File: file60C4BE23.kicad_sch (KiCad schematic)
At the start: 6 parts, among them U10 PCF2123TS_1,118, Y1 32.768kHz

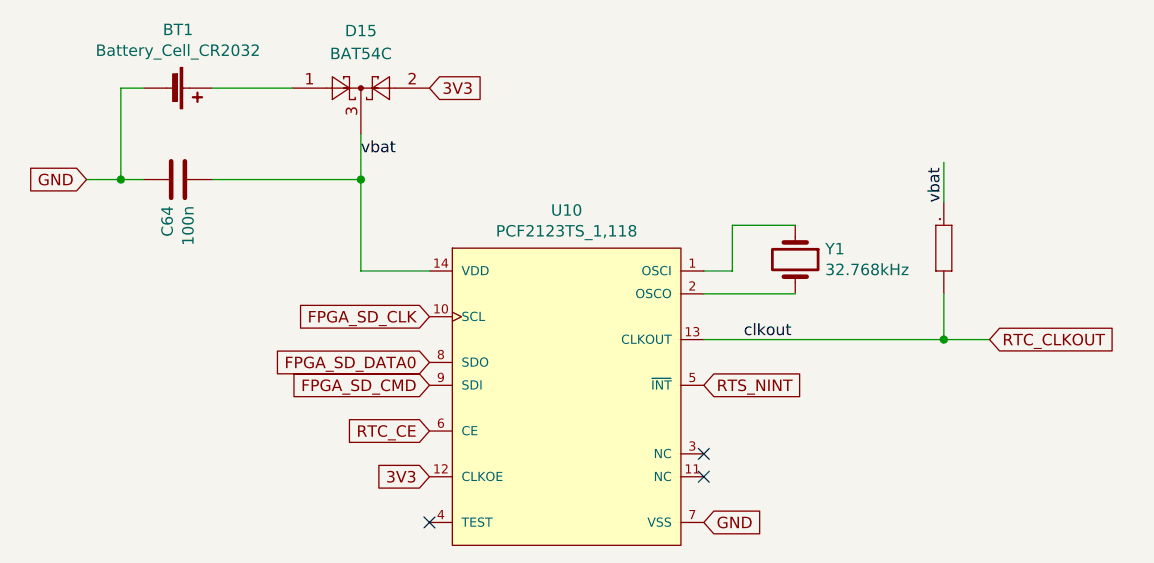
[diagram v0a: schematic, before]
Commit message: Prod version of OpenAARS 5.0 design.
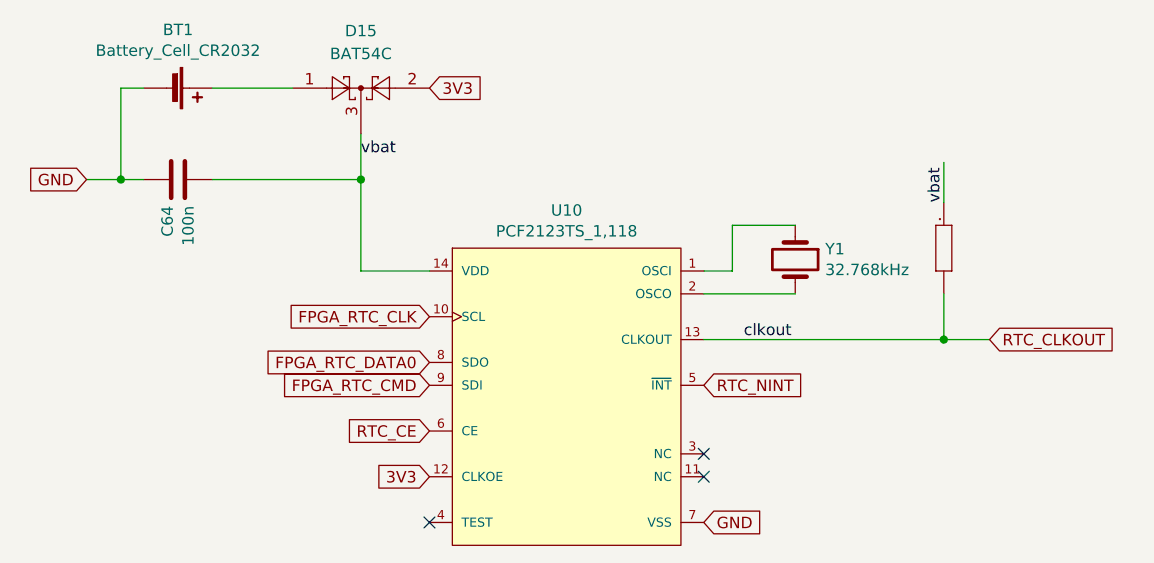
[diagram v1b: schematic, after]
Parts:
- Y1: footprint qmtech-minimig-new:CM7VT1A32768k125pF20PPMTBQA -> CM7VT1A-32768.KiCad:CM7V32768TBQA020
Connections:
- net FPGA_SD_CLK renamed FPGA_RTC_CLK
- net FPGA_SD_CMD renamed FPGA_RTC_CMD
- net FPGA_SD_DATA0 renamed FPGA_RTC_DATA0
- net RTS_NINT renamed RTC_NINT
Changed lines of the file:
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@@
     )
   )
-  (global_label "RTS_NINT" (shape input) (at 166.37 105.41 0) (fields_autoplaced)
+  (global_label "RTC_NINT" (shape input) (at 166.37 105.41 0) (fields_autoplaced)
     (effects (font (size 1.27 1.27)) (justify left))
+    (property "Intersheetrefs" "${INTERSHEET_REFS}" (at 178.0795 105.41 0)
+      (effects (font (size 1.27 1.27)) (justify left) hide)
+    )
+  )
+  (global_label "FPGA_RTC_DATA0" (shape input) (at 135.89 102.87 180) (fields_autoplaced)
+    (effects (font (size 1.27 1.27)) (justify right))
+    (property "Intersheetrefs" "${INTERSHEET_REFS}" (at 117.1048 102.87 0)
+      (effects (font (size 1.27 1.27)) (justify right) hide)
+    )
+  )
+  (global_label "RTC_CE" (shape input) (at 135.89 110.49 180) (fields_autoplaced)
+    (effects (font (size 1.27 1.27)) (justify right))
     (property "Intersheetrefs" "${INTERSHEET_REFS}" (at 0 0 0)
       (effects (font (size 1.27 1.27)) hide)
     )
   )
-  (global_label "FPGA_SD_DATA0" (shape input) (at 135.89 102.87 180) (fields_autoplaced)
+  (global_label "3V3" (shape input) (at 135.89 115.57 180) (fields_autoplaced)
     (effects (font (size 1.27 1.27)) (justify right))
     (property "Intersheetrefs" "${INTERSHEET_REFS}" (at 0 0 0)
@@
     )
   )
-  (global_label "RTC_CE" (shape input) (at 135.89 110.49 180) (fields_autoplaced)
-    (effects (font (size 1.27 1.27)) (justify right))
-    (property "Intersheetrefs" "${INTERSHEET_REFS}" (at 0 0 0)
-      (effects (font (size 1.27 1.27)) hide)
-    )
-  )
-  (global_label "3V3" (shape input) (at 135.89 115.57 180) (fields_autoplaced)
-    (effects (font (size 1.27 1.27)) (justify right))
-    (property "Intersheetrefs" "${INTERSHEET_REFS}" (at 0 0 0)
-      (effects (font (size 1.27 1.27)) hide)
-    )
-  )
-  (global_label "FPGA_SD_CLK" (shape input) (at 135.89 97.79 180) (fields_autoplaced)
-    (effects (font (size 1.27 1.27)) (justify right))
-    (property "Intersheetrefs" "${INTERSHEET_REFS}" (at 0 0 0)
-      (effects (font (size 1.27 1.27)) hide)
-    )
-  )
-  (global_label "FPGA_SD_CMD" (shape input) (at 135.89 105.41 180) (fields_autoplaced)
-    (effects (font (size 1.27 1.27)) (justify right))
-    (property "Intersheetrefs" "${INTERSHEET_REFS}" (at 0 0 0)
-      (effects (font (size 1.27 1.27)) hide)
+  (global_label "FPGA_RTC_CLK" (shape input) (at 135.89 97.79 180) (fields_autoplaced)
+    (effects (font (size 1.27 1.27)) (justify right))
+    (property "Intersheetrefs" "${INTERSHEET_REFS}" (at 119.161 97.79 0)
+      (effects (font (size 1.27 1.27)) (justify right) hide)
+    )
+  )
+  (global_label "FPGA_RTC_CMD" (shape input) (at 135.89 105.41 180) (fields_autoplaced)
+    (effects (font (size 1.27 1.27)) (justify right))
+    (property "Intersheetrefs" "${INTERSHEET_REFS}" (at 118.7377 105.41 0)
+      (effects (font (size 1.27 1.27)) (justify right) hide)
     )
   )
@@
       (effects (font (size 1.27 1.27)) (justify left))
     )
-    (property "Footprint" "qmtech-minimig-new:CM7VT1A32768k125pF20PPMTBQA" (at 176.53 91.44 0)
-      (effects (font (size 1.27 1.27)) hide)
-    )
+    (property "Footprint" "CM7VT1A-32768.KiCad:CM7V32768TBQA020" (at 176.53 91.44 0)
+      (effects (font (size 1.27 1.27)) hide)
+    )
